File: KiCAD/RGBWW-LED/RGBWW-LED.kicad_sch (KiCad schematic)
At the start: 2 parts

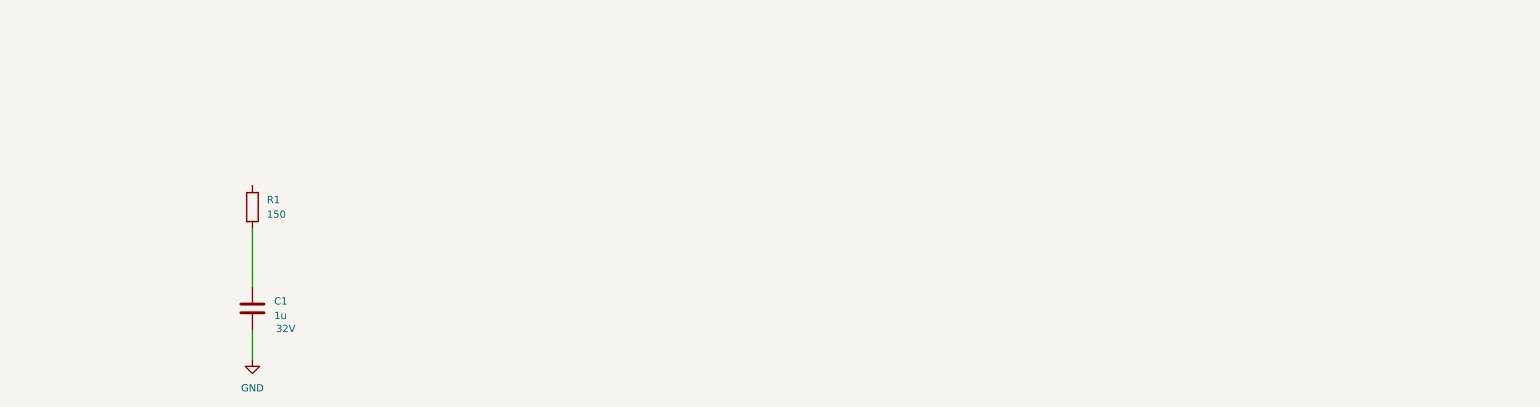
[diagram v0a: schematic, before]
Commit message: added Ledgruppe
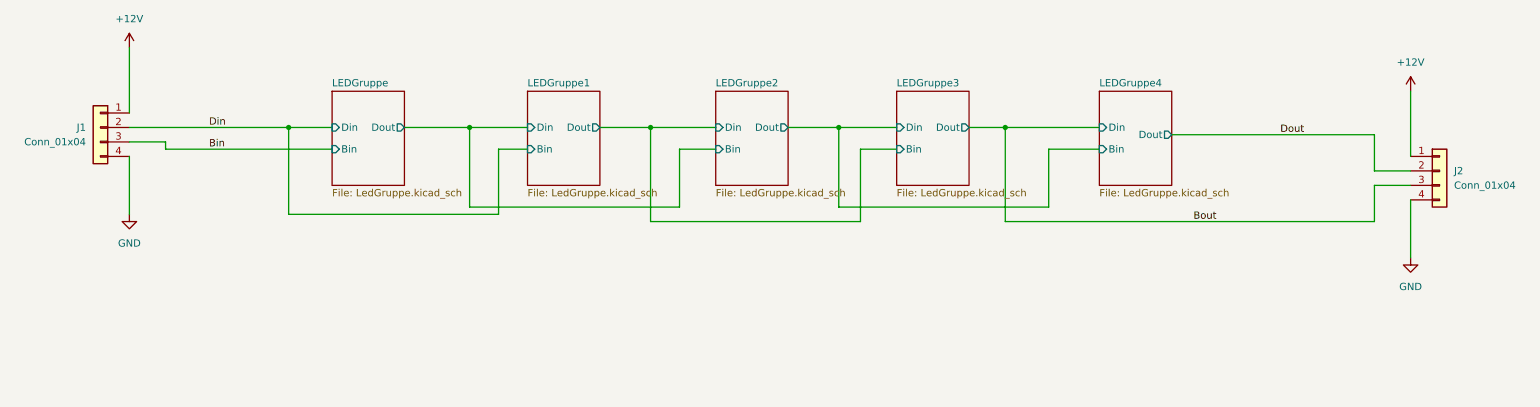
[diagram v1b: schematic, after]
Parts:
- removed C1: 1u, Capacitor_SMD:C_0603_1608Metric, symbol Device:C
- removed R1: 150, Resistor_SMD:R_0603_1608Metric, symbol Device:R
- added J1, J2: Conn_01x04, Connector_PinHeader_2.54mm:PinHeader_1x04_P2.54mm_Horizontal, symbol Connector_Generic:Conn_01x04
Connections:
- net GND: now also J1.4 (Pin_4), J2.4 (Pin_4)
- new net +12V: J1.1 (Pin_1), J2.1 (Pin_1)
- new net Bin: J1.3 (Pin_3)
- new net Bout: J2.3 (Pin_3)
- new net Din: J1.2 (Pin_2)
- new net Dout: J2.2 (Pin_2)
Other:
- added sheet LEDGruppe (LedGruppe.kicad_sch)
- added sheet LEDGruppe1 (LedGruppe.kicad_sch)
- added sheet LEDGruppe2 (LedGruppe.kicad_sch)
- added sheet LEDGruppe3 (LedGruppe.kicad_sch)
- added sheet LEDGruppe4 (LedGruppe.kicad_sch)
- title: RGBWW-LED -> RGBWW Led Gruppen
